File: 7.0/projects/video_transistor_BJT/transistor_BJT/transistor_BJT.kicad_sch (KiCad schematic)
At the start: 6 parts, among them Q1-2N2222A NPN

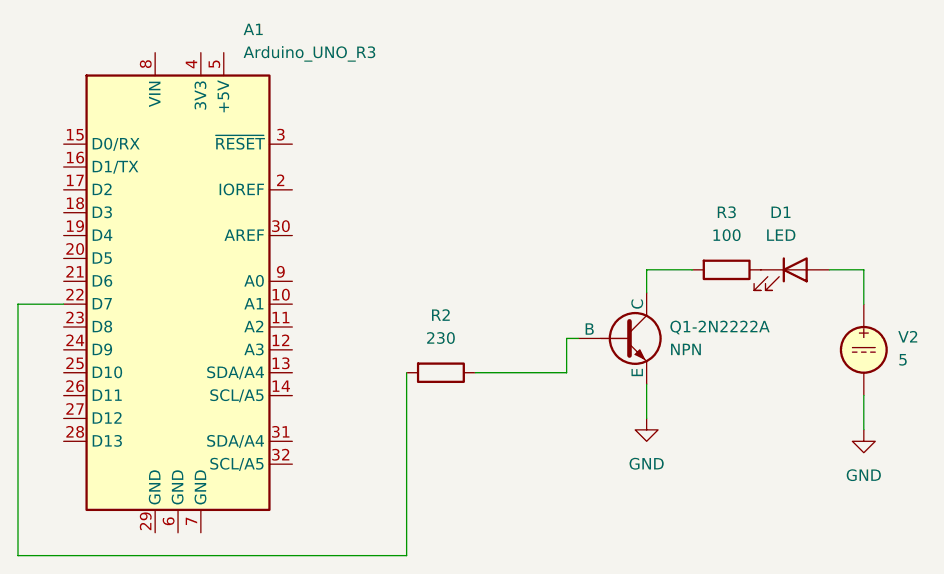
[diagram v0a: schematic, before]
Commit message: adding 555 example
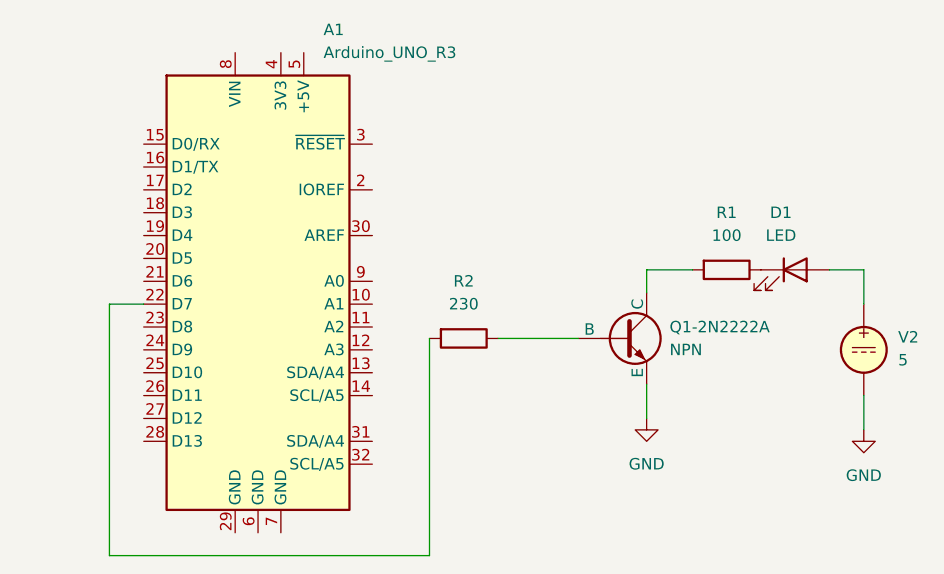
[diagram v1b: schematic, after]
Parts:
- renumbered R3 to R1
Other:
- moved on the sheet: A1, R2
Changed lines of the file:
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@@
 	(wire
 		(pts
-			(xy 95.25 97.79) (xy 85.09 97.79)
+			(xy 87.63 93.98) (xy 96.52 93.98)
 		)
 		(stroke
@@
 	(wire
 		(pts
-			(xy 34.29 118.11) (xy 77.47 118.11)
+			(xy 48.26 90.17) (xy 44.45 90.17)
 		)
 		(stroke
@@
 	(wire
 		(pts
-			(xy 95.25 93.98) (xy 96.52 93.98)
+			(xy 44.45 90.17) (xy 44.45 118.11)
 		)
 		(stroke
@@
 	(wire
 		(pts
-			(xy 104.14 99.06) (xy 104.14 102.87)
+			(xy 44.45 118.11) (xy 80.01 118.11)
 		)
 		(stroke
@@
 	(wire
 		(pts
-			(xy 39.37 90.17) (xy 34.29 90.17)
+			(xy 104.14 99.06) (xy 104.14 102.87)
 		)
 		(stroke
@@
 	(wire
 		(pts
-			(xy 77.47 118.11) (xy 77.47 97.79)
+			(xy 80.01 118.11) (xy 80.01 93.98)
 		)
 		(stroke
@@
 	(wire
 		(pts
-			(xy 95.25 93.98) (xy 95.25 97.79)
+			(xy 109.22 86.36) (xy 104.14 86.36)
 		)
 		(stroke
@@
 	(wire
 		(pts
-			(xy 109.22 86.36) (xy 104.14 86.36)
+			(xy 104.14 86.36) (xy 104.14 88.9)
 		)
 		(stroke
@@
 		)
 	)
-	(wire
-		(pts
-			(xy 34.29 90.17) (xy 34.29 118.11)
-		)
-		(stroke
-			(width 0)
-			(type default)
-		)
-	)
-	(wire
-		(pts
-			(xy 104.14 86.36) (xy 104.14 88.9)
-		)
-		(stroke
-			(width 0)
-			(type default)
-		)
-	)
 	(symbol
 		(lib_id "Device:R")
-		(at 81.28 97.79 270)
+		(at 83.82 93.98 270)
 		(unit 1)
 		(exclude_from_sim no)
@@
 		(fields_autoplaced yes)
 		(property "Reference" "R2"
-			(at 81.28 91.44 90)
+			(at 83.82 87.63 90)
 			(effects
 				(font
@@
 		)
 		(property "Value" "230"
-			(at 81.28 93.98 90)
+			(at 83.82 90.17 90)
 			(effects
 				(font
@@
 		)
 		(property "Footprint" ""
-			(at 81.28 96.012 90)
+			(at 83.82 92.202 90)
 			(effects
 				(font
@@
 		)
 		(property "Datasheet" "~"
-			(at 81.28 97.79 0)
+			(at 83.82 93.98 0)
 			(effects
 				(font
@@
 		)
 		(property "Description" "Resistor"
-			(at 81.28 97.79 0)
+			(at 83.82 93.98 0)
 			(effects
 				(font
@@
 	(symbol
 		(lib_id "MCU_Module:Arduino_UNO_R3")
-		(at 52.07 87.63 0)
+		(at 60.96 87.63 0)
 		(unit 1)
 		(exclude_from_sim no)
@@
 		(fields_autoplaced yes)
 		(property "Reference" "A1"
-			(at 59.3441 59.69 0)
+			(at 68.2341 59.69 0)
 			(effects
 				(font
@@
 		)
 		(property "Value" "Arduino_UNO_R3"
-			(at 59.3441 62.23 0)
+			(at 68.2341 62.23 0)
 			(effects
 				(font
@@
 		)
 		(property "Footprint" "Module:Arduino_UNO_R3"
-			(at 52.07 87.63 0)
+			(at 60.96 87.63 0)
 			(effects
 				(font
@@
 		)
 		(property "Datasheet" "https://www.arduino.cc/en/Main/arduinoBoardUno"
-			(at 52.07 87.63 0)
+			(at 60.96 87.63 0)
 			(effects
 				(font
@@
 		)
 		(property "Description" "Arduino UNO Microcontroller Module, release 3"
-			(at 52.07 87.63 0)
+			(at 60.96 87.63 0)
 			(effects
 				(font
@@
 		(dnp no)
 		(fields_autoplaced yes)
-		(property "Reference" "R3"
+		(property "Reference" "R1"
 			(at 113.03 80.01 90)
 			(effects
@@
 			(project "transistor_BJT"
 				(path "/56d0690a-4f43-41dc-928d-77bd97c5f5f6"
-					(reference "R3")
+					(reference "R1")
 					(unit 1)
 				)
